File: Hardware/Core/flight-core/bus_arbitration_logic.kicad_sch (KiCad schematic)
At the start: 5 parts, among them U4 SN74LVC2G08DCUT, U5 SN74LVC2G132DCTR, U6 SN74LV32APWR, U7 SN74LVC2G07DBVR, U8 SN74LVC2G04DBVR

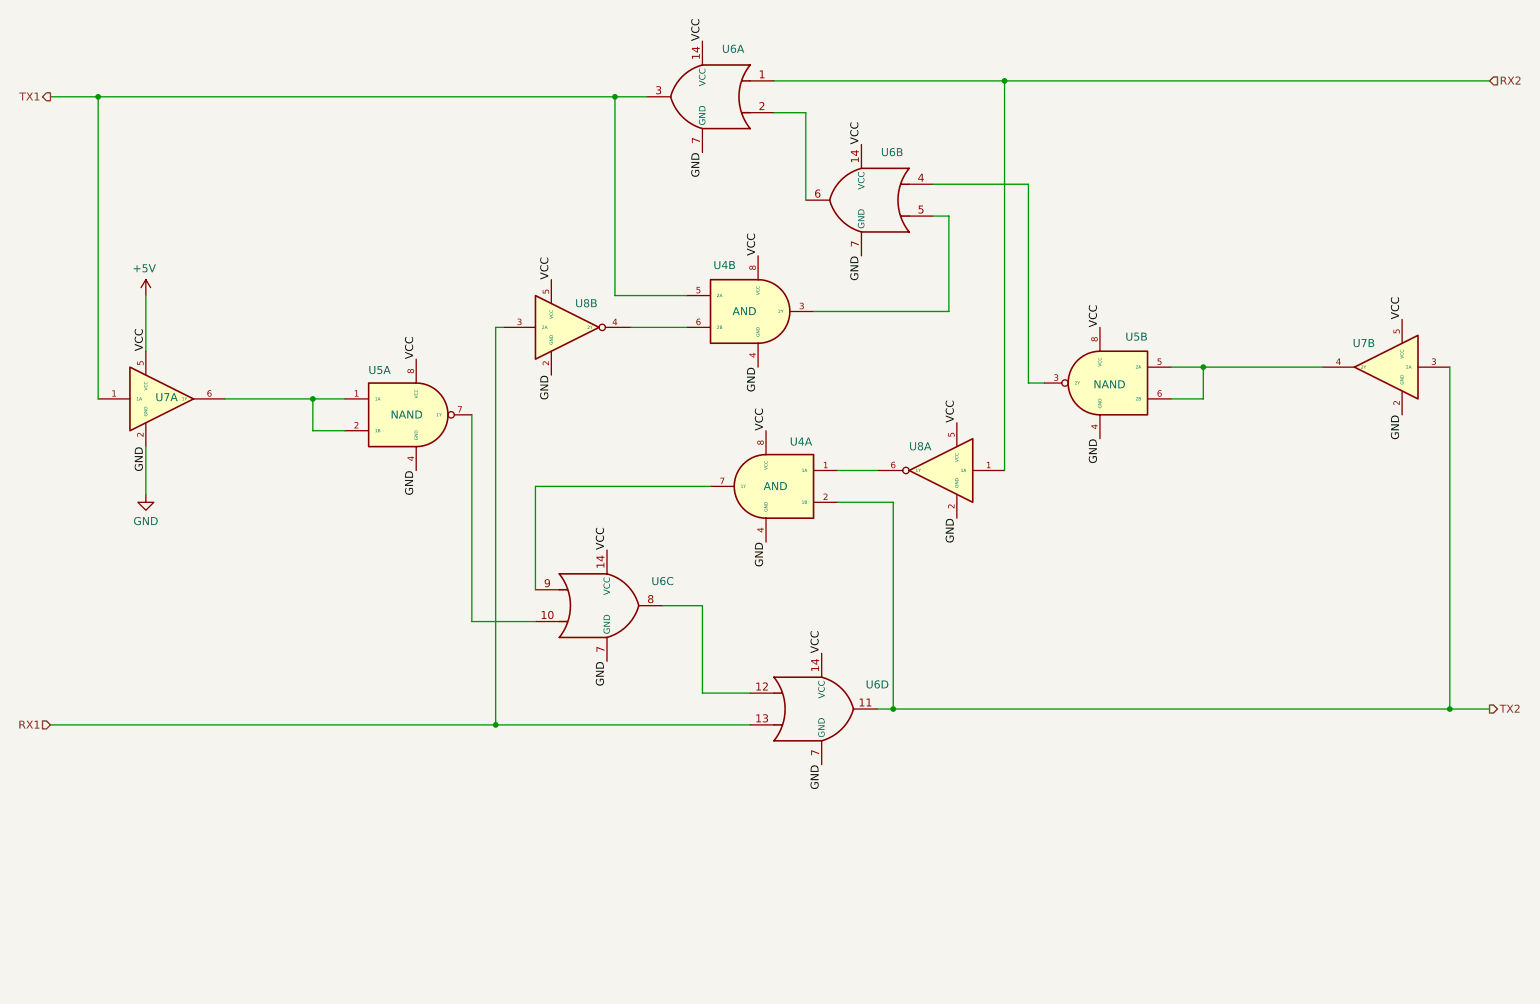
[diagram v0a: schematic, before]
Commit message: moving multi-unit parts into OlinBAD library; added 0603 0.1uF cap
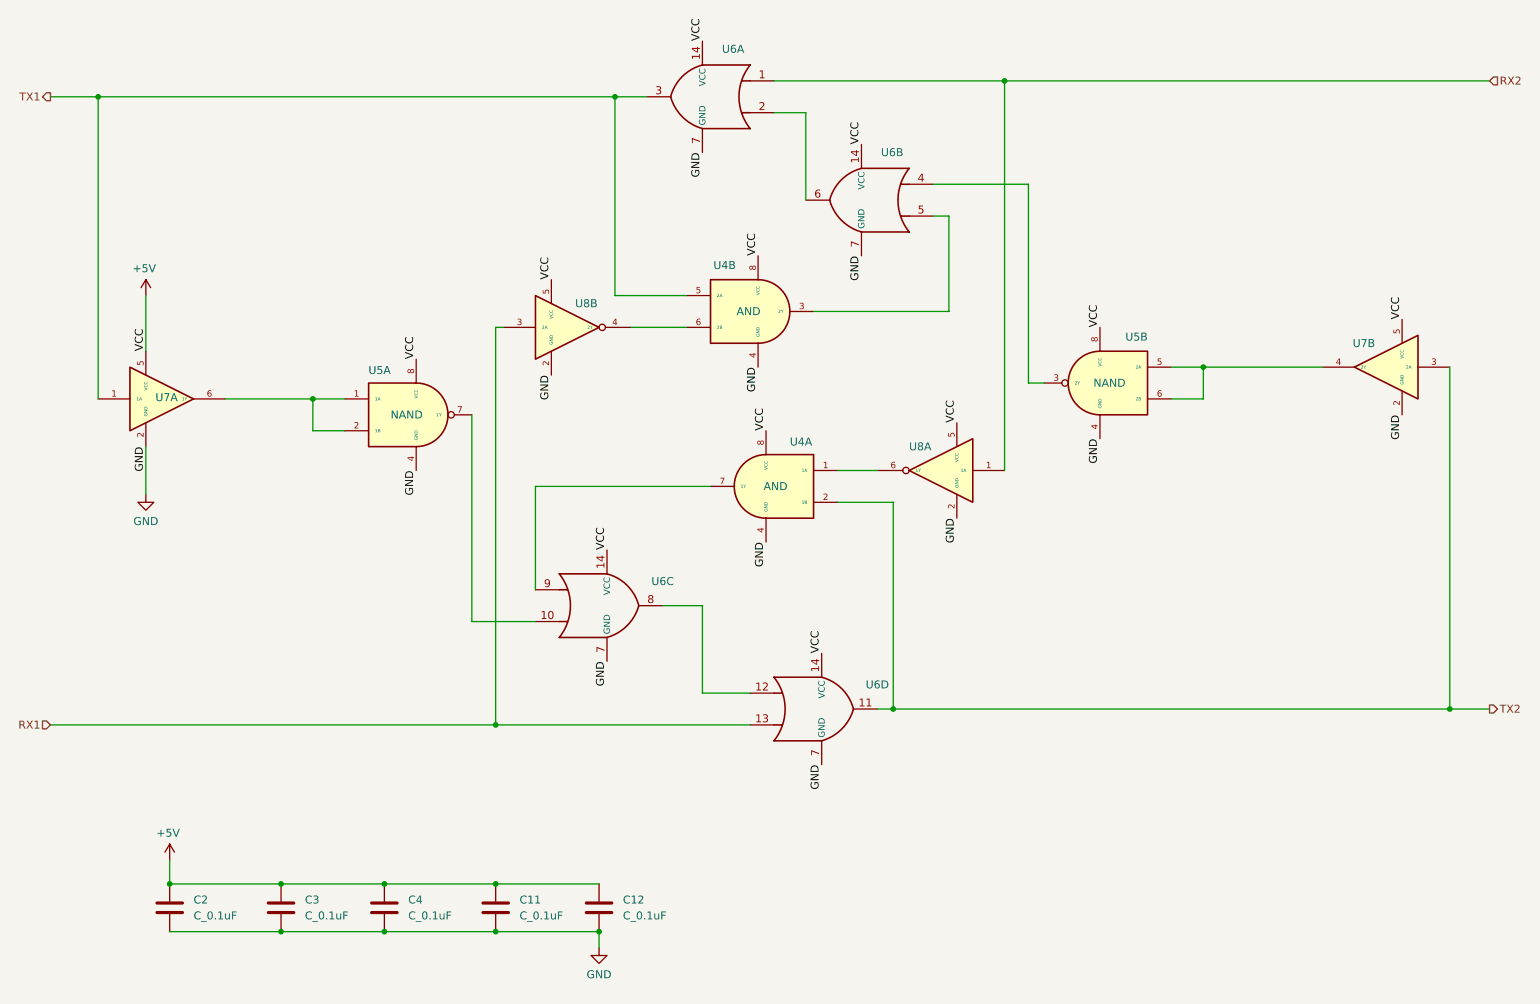
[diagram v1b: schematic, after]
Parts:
- added C11, C12, C2, C3, C4: C_0.1uF, footprints:C_0603_1608Metric, symbol OlinBAD:C_0.1uF_0603
- U4: symbol formula:SN74LVC2G08DCUT_2U_AND -> OlinBAD:SN74LVC2G08DCUT_2U_AND
- U5: symbol formula:SN74LVC2G132DCTR_2U_NAND -> OlinBAD:SN74LVC2G132DCTR_2U_NAND
- U6: symbol formula:SN74LV32APWR_4U_OR -> OlinBAD:SN74LV32APWR_4U_OR
- U7: footprint SN74LVC2G07DBVR:SOT95P280X145-6N -> obad_footprints:SOT95P280X145-6N; symbol formula:SN74LVC2G07DBVR_MultiUnit -> OlinBAD:SN74LVC2G07DBVR_2U_Buffer
- U8: symbol formula:SN74LVC2G04DBVR_2U_Inverter -> OlinBAD:SN74LVC2G04DBVR_2U_Inverter
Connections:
- net +5V: now also C11.1, C12.1, C2.1, C3.1, C4.1
- net GND: now also C11.2, C12.2, C2.2, C3.2, C4.2

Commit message: Removed images, added 3.3V and 5V hierarchical inputs, added second pair of decoupling caps
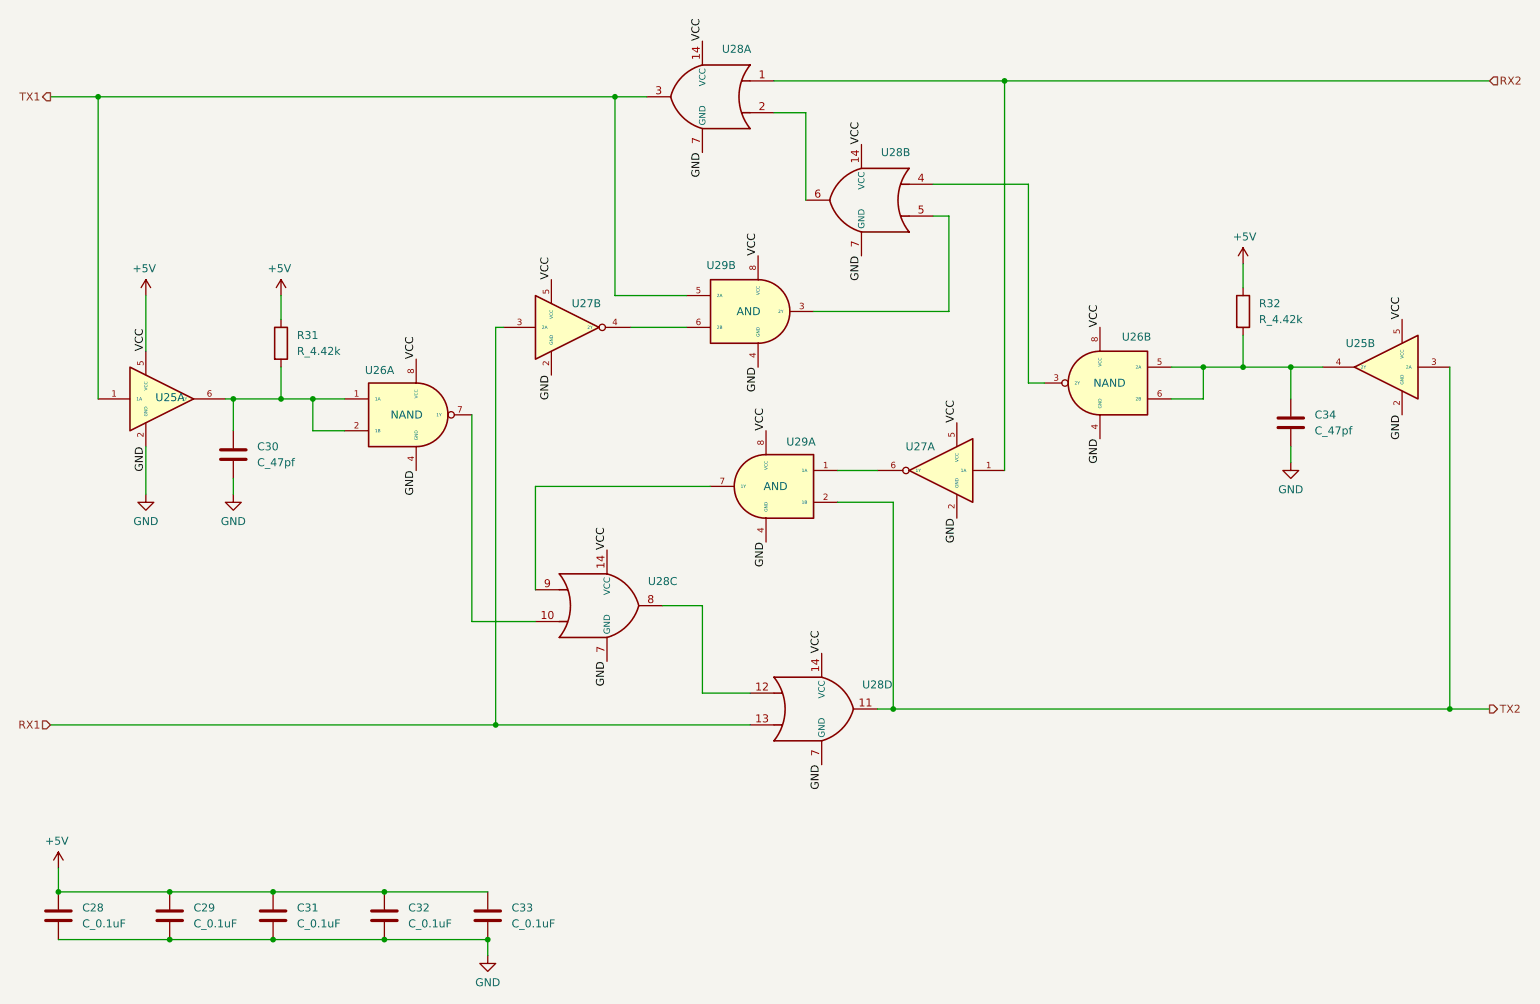
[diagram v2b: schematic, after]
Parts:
- added C30, C34: C_47pf, footprints:C_0603_1608Metric, symbol Device:C
- added R31, R32: R_4.42k, footprints:R_0603_1608Metric, symbol Device:R
- renumbered C2 to C28, C3 to C29, C4 to C31, C11 to C32, C12 to C33, U7 to U25, U5 to U26, U8 to U27, U6 to U28, U4 to U29
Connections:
- net +5V: now also R31.1, R32.1
- net GND: now also C30.2, C34.2
- net at U25.4 (2Y), U26.5 (2A), U26.6 (2B): now also C34.1, R32.2
- net at U25.6 (1Y), U26.1 (1A), U26.2 (1B): now also C30.1, R31.2
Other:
- moved on the sheet: C28, C29, C31, C32, C33

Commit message: renaming the values of LRC generics to just the value with unit letter (except resistors are just the value)
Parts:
- removed C29, C31, C32, C33: C_0.1uF, footprints:C_0603_1608Metric, symbol OlinBAD:C_0.1uF_0603
- added C118, C124, C47, C67, C91: 0.1uF, footprints:C_0603_1608Metric, symbol OlinBAD:C_0.1uF_0603
- C101: renamed from C30; value C_47pf -> 47pF
- C152: renamed from C34; value C_47pf -> 47pF
- C28: value C_0.1uF -> 0.1uF
- renumbered R31 to R52, R32 to R53, U25 to U68, U26 to U69, U27 to U77, U28 to U78, U29 to U79
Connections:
- net +5V: now also C118.1, C124.1, C47.1, C67.1, C91.1
- net GND: now also C118.2, C124.2, C47.2, C67.2, C91.2

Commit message: minor erc fixes (grid, reannotation, updated footprint associations)
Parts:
- removed C124: 0.1uF, footprints:C_0603_1608Metric, symbol OlinBAD:C_0.1uF_0603
- added C22: 0.1uF, footprints:C_0603_1608Metric, symbol OlinBAD:C_0.1uF_0603
- renumbered C28 to C23, C47 to C24, C101 to C25, C67 to C26, C91 to C27, C118 to C28, C152 to C29, R52 to R13, R53 to R14, U77 to U10, U78 to U11, U79 to U12, U68 to U8, U69 to U9
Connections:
- net +5V: now also C22.1
- net GND: now also C22.2

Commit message: completed can repeater layout, swapped gate pins for layout convenience
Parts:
- removed C28: 0.1uF, footprints:C_0603_1608Metric, symbol OlinBAD:C_0.1uF_0603
- renumbered C29 to C28, R13 to R14, R14 to R15
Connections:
- net RX1: now also U10.1 (1A); no longer U10.3 (2A)
- net RX2: now also U10.3 (2A); no longer U10.1 (1A)
- net TX1: now also U12.6 (2B); no longer U12.5 (2A)
- net at C28.1, R15.2, U8.4 (2Y): now also U9.1 (1A), U9.2 (1B); no longer U9.5 (2A), U9.6 (2B)
- net at U11.4: now also U9.7 (1Y); no longer U9.3 (2Y)
- net at U10.6 (1Y): now also U12.5 (2A); no longer U12.1 (1A)
- net at C25.1, R14.2, U8.6 (1Y): now also U9.5 (2A), U9.6 (2B); no longer U9.1 (1A), U9.2 (1B)
- net at U10.4 (2Y): now also U12.1 (1A); no longer U12.6 (2B)
- net at U11.10: now also U9.3 (2Y); no longer U9.7 (1Y)
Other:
- moved on the sheet: U10A, U10B, U9A, U9B
